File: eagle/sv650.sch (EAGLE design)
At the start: 20 parts, among them IC1 7805

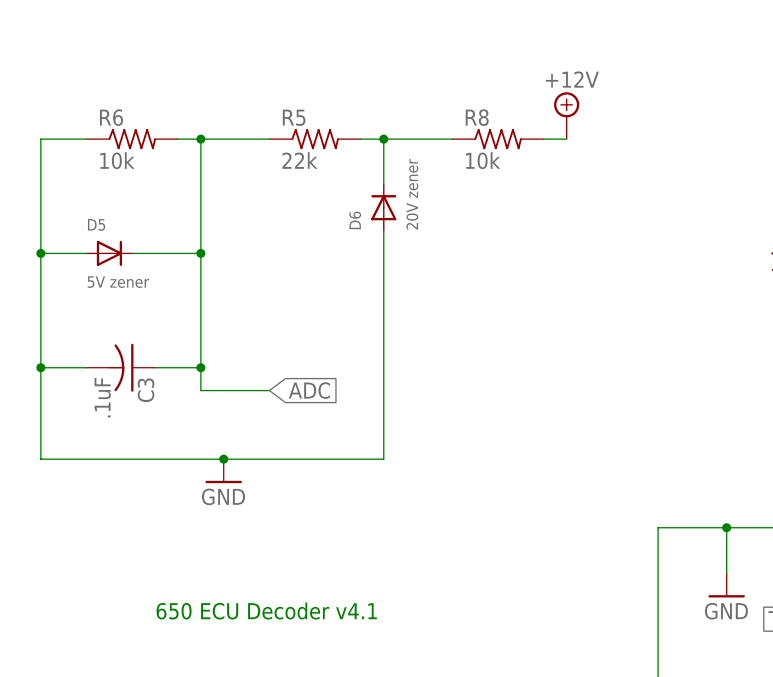
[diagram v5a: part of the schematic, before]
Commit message: remove 20V zener replace 5V zener with 4.7V zener (hard to find 5V zeners) merge 10K + 22K into a single 30K resistor clean up traces & remove lots of vias
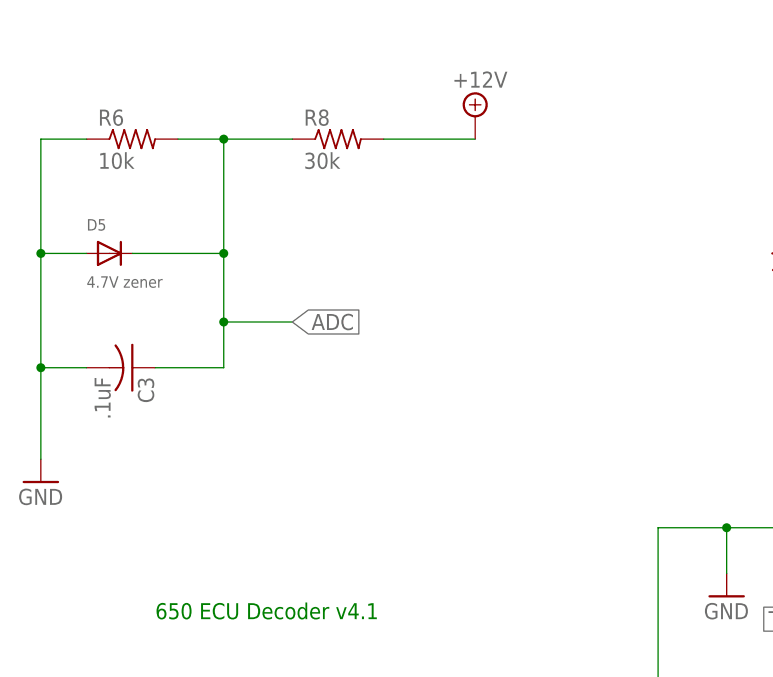
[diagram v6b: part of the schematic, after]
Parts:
- removed D6: 20V zener, adafruit:DIODESOD-123
- removed R5: 22k, resistor:R-US_M0805
- D5: value 5V zener -> 4.7V zener
- R8: value 10k -> 30k
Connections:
- removed net N$13: D6.C, R5.2, R8.1
- net ADC: now also R8.1; no longer R5.1
- net GND: no longer D6.A
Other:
- moved on the sheet: R8
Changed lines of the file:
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@@
 <attribute name="OC_NEWARK" value="unknown"/>
-</part>
-<part name="R5" library="resistor" deviceset="R-US_" device="M0805" value="22k">
-<attribute name="MF" value=""/>
-<attribute name="MPN" value="CRCW080522K0FKEA"/>
-<attribute name="OC_NEWARK" value="61M5466"/>
 </part>
 <part name="R6" library="resistor" deviceset="R-US_" device="M0805" value="10k">
@@
 <part name="SUPPLY1" library="supply2" deviceset="+12V" device=""/>
 <part name="SUPPLY2" library="supply2" deviceset="+12V" device=""/>
-<part name="R8" library="resistor" deviceset="R-US_" device="M0805" value="10k">
+<part name="R8" library="resistor" deviceset="R-US_" device="M0805" value="30k">
 <attribute name="MF" value="VISHAY/DALE"/>
 <attribute name="MPN" value="CRCW080510K0FKTA"/>
 <attribute name="OC_NEWARK" value="05F1511"/>
 </part>
-<part name="D6" library="adafruit" deviceset="DIODE" device="SOD-123" value="20V zener">
-<attribute name="MF" value="VISHAY/TELEFUNKEN"/>
-<attribute name="MPN" value="MMSZ5242B-V-GS08"/>
-<attribute name="OC_NEWARK" value="35K8677"/>
-</part>
 <part name="SUPPLY3" library="supply2" deviceset="+12V" device=""/>
 <part name="GND2" library="SparkFun" deviceset="GND" device=""/>
-<part name="D5" library="adafruit" deviceset="DIODE" device="SOD-123" value="5V zener">
-<attribute name="MF" value="VISHAY/TELEFUNKEN"/>
-<attribute name="MPN" value="MMSZ5242B-V-GS08"/>
-<attribute name="OC_NEWARK" value="35K8677"/>
-</part>
 <part name="C3" library="adafruit" deviceset="C-US" device="025-024X044" value=".1uF">
 <attribute name="MF" value=""/>
 <attribute name="MPN" value=""/>
 <attribute name="OC_NEWARK" value="unknown"/>
+</part>
+<part name="D5" library="adafruit" deviceset="DIODE" device="SOD-123" value="4.7V zener">
+<attribute name="MF" value="VISHAY/TELEFUNKEN"/>
+<attribute name="MPN" value="MMSZ5242B-V-GS08"/>
+<attribute name="OC_NEWARK" value="35K8677"/>
 </part>
 </parts>
@@
 <attribute name="MPN" x="121.92" y="10.16" size="1.778" layer="96" display="off"/>
 </instance>
-<instance part="R5" gate="G$1" x="2.54" y="101.6">
-<attribute name="OC_NEWARK" x="2.54" y="101.6" size="1.778" layer="96" display="off"/>
-<attribute name="MF" x="2.54" y="101.6" size="1.778" layer="96" display="off"/>
-<attribute name="MPN" x="2.54" y="101.6" size="1.778" layer="96" display="off"/>
-</instance>
 <instance part="R6" gate="G$1" x="-17.78" y="101.6">
 <attribute name="OC_NEWARK" x="-17.78" y="101.6" size="1.778" layer="96" display="off"/>
@@
 <instance part="U$9" gate="G$1" x="25.4" y="15.24"/>
 <instance part="GND1" gate="1" x="48.26" y="50.8"/>
-<instance part="SUPPLY1" gate="+12V" x="30.48" y="104.14"/>
+<instance part="SUPPLY1" gate="+12V" x="20.32" y="104.14"/>
 <instance part="SUPPLY2" gate="+12V" x="55.88" y="101.6"/>
-<instance part="R8" gate="G$1" x="22.86" y="101.6">
-<attribute name="OC_NEWARK" x="22.86" y="101.6" size="1.778" layer="96" display="off"/>
-<attribute name="MF" x="22.86" y="101.6" size="1.778" layer="96" display="off"/>
-<attribute name="MPN" x="22.86" y="101.6" size="1.778" layer="96" display="off"/>
-</instance>
-<instance part="D6" gate="G$1" x="10.16" y="93.98" rot="R90">
-<attribute name="OC_NEWARK" x="10.16" y="93.98" size="1.778" layer="96" display="off"/>
-<attribute name="MF" x="10.16" y="93.98" size="1.778" layer="96" display="off"/>
-<attribute name="MPN" x="10.16" y="93.98" size="1.778" layer="96" display="off"/>
+<instance part="R8" gate="G$1" x="5.08" y="101.6">
+<attribute name="OC_NEWARK" x="5.08" y="101.6" size="1.778" layer="96" display="off"/>
+<attribute name="MF" x="5.08" y="101.6" size="1.778" layer="96" display="off"/>
+<attribute name="MPN" x="5.08" y="101.6" size="1.778" layer="96" display="off"/>
 </instance>
 <instance part="SUPPLY3" gate="+12V" x="154.94" y="109.22"/>
-<instance part="GND2" gate="1" x="-7.62" y="63.5"/>
+<instance part="GND2" gate="1" x="-27.94" y="63.5"/>
+<instance part="C3" gate="G$1" x="-17.78" y="76.2" rot="R270">
+<attribute name="OC_NEWARK" x="-17.78" y="76.2" size="1.778" layer="96" rot="R270" display="off"/>
+<attribute name="MF" x="-17.78" y="76.2" size="1.778" layer="96" rot="R270" display="off"/>
+<attribute name="MPN" x="-17.78" y="76.2" size="1.778" layer="96" rot="R270" display="off"/>
+</instance>
 <instance part="D5" gate="G$1" x="-20.32" y="88.9">
 <attribute name="OC_NEWARK" x="-20.32" y="88.9" size="1.778" layer="96" rot="R270" display="off"/>
 <attribute name="MF" x="-20.32" y="88.9" size="1.778" layer="96" rot="R270" display="off"/>
 <attribute name="MPN" x="-20.32" y="88.9" size="1.778" layer="96" rot="R270" display="off"/>
-</instance>
-<instance part="C3" gate="G$1" x="-17.78" y="76.2" rot="R270">
-<attribute name="OC_NEWARK" x="-17.78" y="76.2" size="1.778" layer="96" rot="R270" display="off"/>
-<attribute name="MF" x="-17.78" y="76.2" size="1.778" layer="96" rot="R270" display="off"/>
-<attribute name="MPN" x="-17.78" y="76.2" size="1.778" layer="96" rot="R270" display="off"/>
 </instance>
 </instances>
@@
 </segment>
 <segment>
-<wire x1="-27.94" y1="66.04" x2="-7.62" y2="66.04" width="0.1524" layer="91"/>
-<pinref part="D6" gate="G$1" pin="A"/>
-<wire x1="-7.62" y1="66.04" x2="10.16" y2="66.04" width="0.1524" layer="91"/>
-<wire x1="10.16" y1="66.04" x2="10.16" y2="91.44" width="0.1524" layer="91"/>
 <pinref part="GND2" gate="1" pin="GND"/>
-<junction x="-7.62" y="66.04"/>
+<pinref part="C3" gate="G$1" pin="2"/>
+<pinref part="D5" gate="G$1" pin="A"/>
 <pinref part="R6" gate="G$1" pin="1"/>
 <wire x1="-22.86" y1="101.6" x2="-27.94" y2="101.6" width="0.1524" layer="91"/>
 <wire x1="-27.94" y1="101.6" x2="-27.94" y2="88.9" width="0.1524" layer="91"/>
-<pinref part="D5" gate="G$1" pin="A"/>
-<wire x1="-22.86" y1="88.9" x2="-27.94" y2="88.9" width="0.1524" layer="91"/>
+<wire x1="-27.94" y1="88.9" x2="-22.86" y2="88.9" width="0.1524" layer="91"/>
 <wire x1="-27.94" y1="88.9" x2="-27.94" y2="76.2" width="0.1524" layer="91"/>
-<pinref part="C3" gate="G$1" pin="2"/>
+<wire x1="-27.94" y1="76.2" x2="-22.86" y2="76.2" width="0.1524" layer="91"/>
 <wire x1="-27.94" y1="76.2" x2="-27.94" y2="66.04" width="0.1524" layer="91"/>
-<wire x1="-27.94" y1="76.2" x2="-22.86" y2="76.2" width="0.1524" layer="91"/>
+<junction x="-27.94" y="88.9"/>
 <junction x="-27.94" y="76.2"/>
-<junction x="-27.94" y="88.9"/>
 </segment>
 </net>
@@
 <net name="+12V" class="0">
 <segment>
-<wire x1="27.94" y1="101.6" x2="30.48" y2="101.6" width="0.1524" layer="91"/>
+<wire x1="10.16" y1="101.6" x2="20.32" y2="101.6" width="0.1524" layer="91"/>
 <pinref part="SUPPLY1" gate="+12V" pin="+12V"/>
 <pinref part="R8" gate="G$1" pin="2"/>
@@
 </segment>
 <segment>
-<pinref part="R5" gate="G$1" pin="1"/>
+<pinref part="C3" gate="G$1" pin="1"/>
+<wire x1="-7.62" y1="101.6" x2="0" y2="101.6" width="0.1524" layer="91"/>
+<wire x1="-7.62" y1="101.6" x2="-7.62" y2="88.9" width="0.1524" layer="91"/>
+<wire x1="-7.62" y1="88.9" x2="-7.62" y2="81.28" width="0.1524" layer="91"/>
+<wire x1="-7.62" y1="81.28" x2="-7.62" y2="76.2" width="0.1524" layer="91"/>
+<wire x1="-7.62" y1="76.2" x2="-15.24" y2="76.2" width="0.1524" layer="91"/>
+<label x="0" y="81.28" size="1.778" layer="95" xref="yes"/>
+<pinref part="R8" gate="G$1" pin="1"/>
+<wire x1="-17.78" y1="88.9" x2="-7.62" y2="88.9" width="0.1524" layer="91"/>
 <pinref part="R6" gate="G$1" pin="2"/>
-<wire x1="-2.54" y1="101.6" x2="-10.16" y2="101.6" width="0.1524" layer="91"/>
-<label x="-2.54" y="73.66" size="1.778" layer="95" xref="yes"/>
-<wire x1="-10.16" y1="101.6" x2="-12.7" y2="101.6" width="0.1524" layer="91"/>
-<junction x="-10.16" y="101.6"/>
-<wire x1="-10.16" y1="73.66" x2="-2.54" y2="73.66" width="0.1524" layer="91"/>
-<wire x1="-10.16" y1="101.6" x2="-10.16" y2="88.9" width="0.1524" layer="91"/>
+<wire x1="-12.7" y1="101.6" x2="-7.62" y2="101.6" width="0.1524" layer="91"/>
+<wire x1="0" y1="81.28" x2="-7.62" y2="81.28" width="0.1524" layer="91"/>
 <pinref part="D5" gate="G$1" pin="C"/>
-<wire x1="-10.16" y1="88.9" x2="-10.16" y2="76.2" width="0.1524" layer="91"/>
-<wire x1="-10.16" y1="76.2" x2="-10.16" y2="73.66" width="0.1524" layer="91"/>
-<wire x1="-10.16" y1="88.9" x2="-17.78" y2="88.9" width="0.1524" layer="91"/>
-<junction x="-10.16" y="88.9"/>
-<junction x="-10.16" y="76.2"/>
-<pinref part="C3" gate="G$1" pin="1"/>
-<wire x1="-10.16" y1="76.2" x2="-15.24" y2="76.2" width="0.1524" layer="91"/>
-</segment>
-</net>
-<net name="N$13" class="0">
-<segment>
-<pinref part="R5" gate="G$1" pin="2"/>
-<pinref part="R8" gate="G$1" pin="1"/>
-<wire x1="7.62" y1="101.6" x2="10.16" y2="101.6" width="0.1524" layer="91"/>
-<pinref part="D6" gate="G$1" pin="C"/>
-<wire x1="10.16" y1="101.6" x2="17.78" y2="101.6" width="0.1524" layer="91"/>
-<wire x1="10.16" y1="96.52" x2="10.16" y2="101.6" width="0.1524" layer="91"/>
-<junction x="10.16" y="101.6"/>
-</segment>
-</net>
+<junction x="-7.62" y="81.28"/>
+<junction x="-7.62" y="88.9"/>
+<junction x="-7.62" y="101.6"/>
+</segment>
+</net>
